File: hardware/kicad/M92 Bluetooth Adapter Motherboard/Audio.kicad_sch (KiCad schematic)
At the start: 32 parts, among them IC10 NJU7031D, IC5 NJU7031D, IC6 MAX4619CSE+, IC7 MCP4151-103E/SN, IC8 INA105KU/2K5G4, IC9 INA105KU/2K5G4, J3 Conn_External_Mic, Q1 PN2222ATA

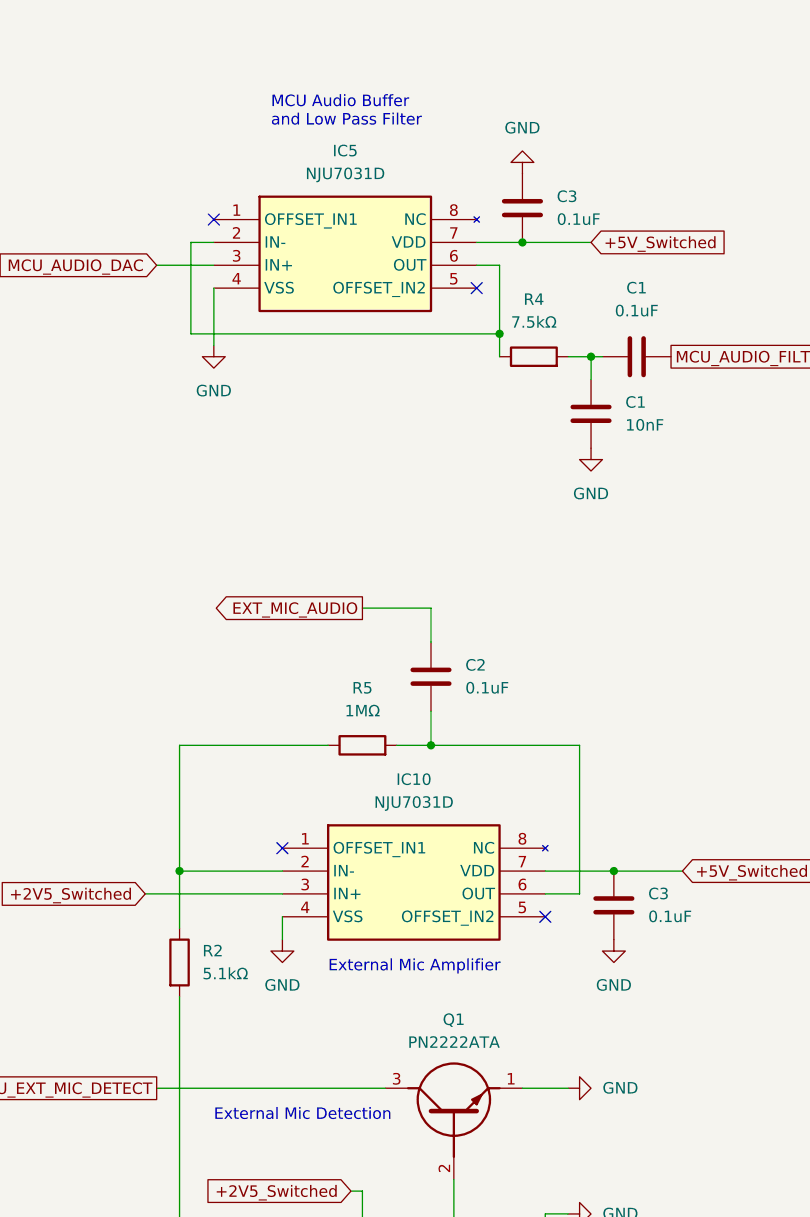
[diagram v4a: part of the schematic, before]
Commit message: Rework load switch enable circuitry/code
Rework load switch enable circuitry/code to fix brief power-on glitch when initially connecting battery power.
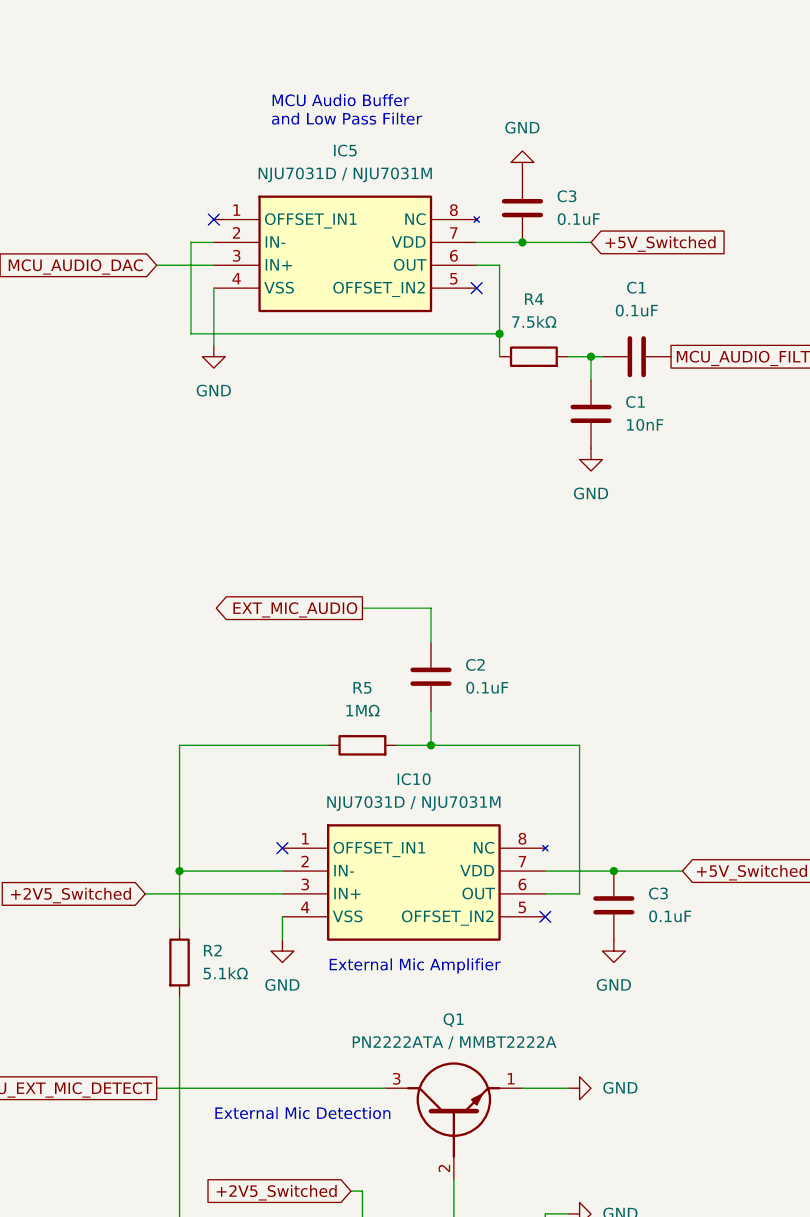
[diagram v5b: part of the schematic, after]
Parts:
- IC10, IC5: value NJU7031D -> NJU7031D / NJU7031M
- Q1: value PN2222ATA -> PN2222ATA / MMBT2222A
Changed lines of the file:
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@@
       (effects (font (size 1.27 1.27)))
     )
-    (property "Value" "NJU7031D" (at 66.675 36.83 0)
+    (property "Value" "NJU7031D / NJU7031M" (at 66.675 36.83 0)
       (effects (font (size 1.27 1.27)))
     )
@@
       (effects (font (size 1.27 1.27)))
     )
-    (property "Value" "PN2222ATA" (at 78.74 133.35 90)
+    (property "Value" "PN2222ATA / MMBT2222A" (at 78.74 133.35 90)
       (effects (font (size 1.27 1.27)))
     )
@@
       (effects (font (size 1.27 1.27)))
     )
-    (property "Value" "NJU7031D" (at 74.295 106.68 0)
-      (effects (font (size 1.27 1.27)))
-    )
+    (property "Value" "NJU7031D / NJU7031M" (at 74.295 106.68 0)
+      (effects (font (size 1.27 1.27)))
+    )

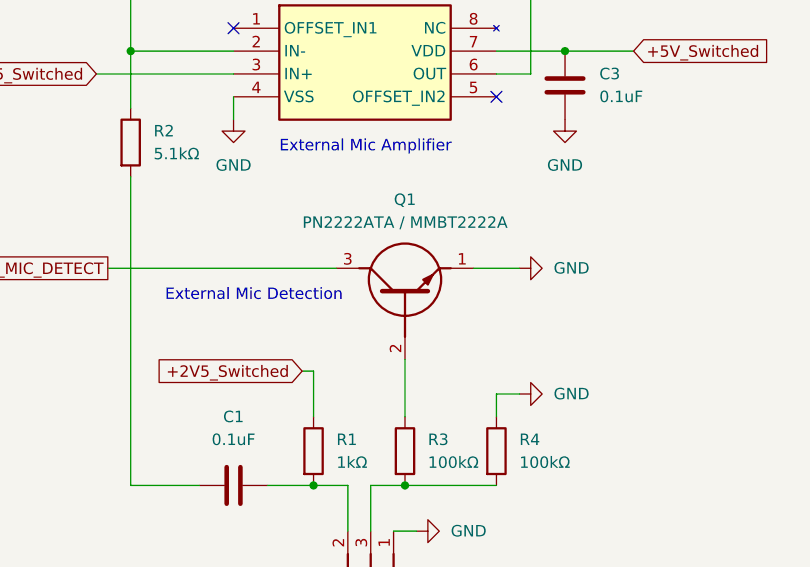
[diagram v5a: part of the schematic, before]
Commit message: Add new battery module to motherboard schematic
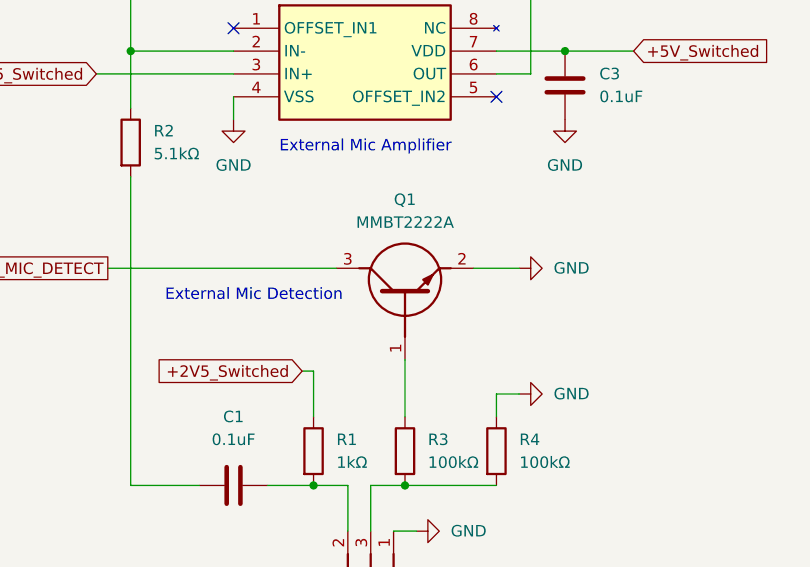
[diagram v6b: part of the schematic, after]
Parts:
- Q1: value PN2222ATA / MMBT2222A -> MMBT2222A; footprint BC33740TA -> Package_TO_SOT_SMD:SOT-23-3; symbol SamacSys_Parts:PN2222ATA -> M92 Bluetooth Adapter Motherboard:BJT_N_BEC; JLCPCB Part # (none) -> C8512; Manufacturer (none) -> JCST; Manufacturer_Name onsemi -> (none); Manufacturer_Part_Number PN2222ATA -> MMBT2222A; Mouser Part Number 512-PN2222ATA -> (none); Mouser Price/Stock https://www.mouser.com/ProductDetail/onsemi-Fairchild/PN222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 -> (none)
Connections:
- net GND: now also Q1.2 (E); no longer Q1.1 (E)
- net at R3.1: now also Q1.1 (B); no longer Q1.2 (B)
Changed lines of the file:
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@@
     )
   )
-  (symbol (lib_id "SamacSys_Parts:PN2222ATA") (at 78.74 148.59 90) (unit 1)
+  (symbol (lib_id "M92 Bluetooth Adapter Motherboard:BJT_N_BEC") (at 78.74 148.59 90) (unit 1)
     (in_bom yes) (on_board yes) (dnp no) (fields_autoplaced)
     (property "Reference" "Q1" (at 78.74 130.81 90)
       (effects (font (size 1.27 1.27)))
     )
-    (property "Value" "PN2222ATA / MMBT2222A" (at 78.74 133.35 90)
+    (property "Value" "MMBT2222A" (at 78.74 133.35 90)
       (effects (font (size 1.27 1.27)))
     )
-    (property "Footprint" "BC33740TA" (at 180.01 134.62 0)
-      (effects (font (size 1.27 1.27)) (justify left top) hide)
+    (property "Footprint" "Package_TO_SOT_SMD:SOT-23-3" (at 78.74 148.59 0)
+      (effects (font (size 1.27 1.27)) hide)
     )
-    (property "Datasheet" "https://www.mouser.com/datasheet/2/308/1/PN2222A_D-2319791.pdf" (at 280.01 134.62 0)
-      (effects (font (size 1.27 1.27)) (justify left top) hide)
+    (property "Datasheet" "https://www.lcsc.com/datasheet/lcsc_datasheet_1811081957_Jiangsu-Changjing-Electronics-Technology-Co---Ltd--MMBT2222A-1P_C8512.pdf" (at 78.74 148.59 0)
+      (effects (font (size 1.27 1.27)) hide)
     )
     (property "Height" "" (at 480.01 134.62 0)
       (effects (font (size 1.27 1.27)) (justify left top) hide)
     )
-    (property "Mouser Part Number" "512-PN2222ATA" (at 580.01 134.62 0)
+    (property "Mouser Part Number" "" (at 580.01 134.62 0)
       (effects (font (size 1.27 1.27)) (justify left top) hide)
     )
-    (property "Mouser Price/Stock" "https://www.mouser.com/ProductDetail/onsemi-Fairchild/PN2222ATA?qs=QwEULm8S1DrfA%2FCRPqYa%252Bw%3D%3D" (at 680.01 134.62 0)
+    (property "Mouser Price/Stock" "" (at 680.01 134.62 0)
       (effects (font (size 1.27 1.27)) (justify left top) hide)
     )
-    (property "Manufacturer_Name" "onsemi" (at 780.01 134.62 0)
+    (property "Manufacturer_Name" "" (at 780.01 134.62 0)
       (effects (font (size 1.27 1.27)) (justify left top) hide)
     )
-    (property "Manufacturer_Part_Number" "PN2222ATA" (at 880.01 134.62 0)
+    (property "Manufacturer_Part_Number" "MMBT2222A" (at 880.01 134.62 0)
       (effects (font (size 1.27 1.27)) (justify left top) hide)
     )
-    (property "JLCPCB Part #" "" (at 78.74 148.59 0)
+    (property "JLCPCB Part #" "C8512" (at 78.74 148.59 0)
       (effects (font (size 1.27 1.27)) hide)
     )
+    (property "Manufacturer" "JCST" (at 78.74 148.59 0)
+      (effects (font (size 1.27 1.27)) hide)
+    )
